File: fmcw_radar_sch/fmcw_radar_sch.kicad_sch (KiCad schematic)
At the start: 0 parts

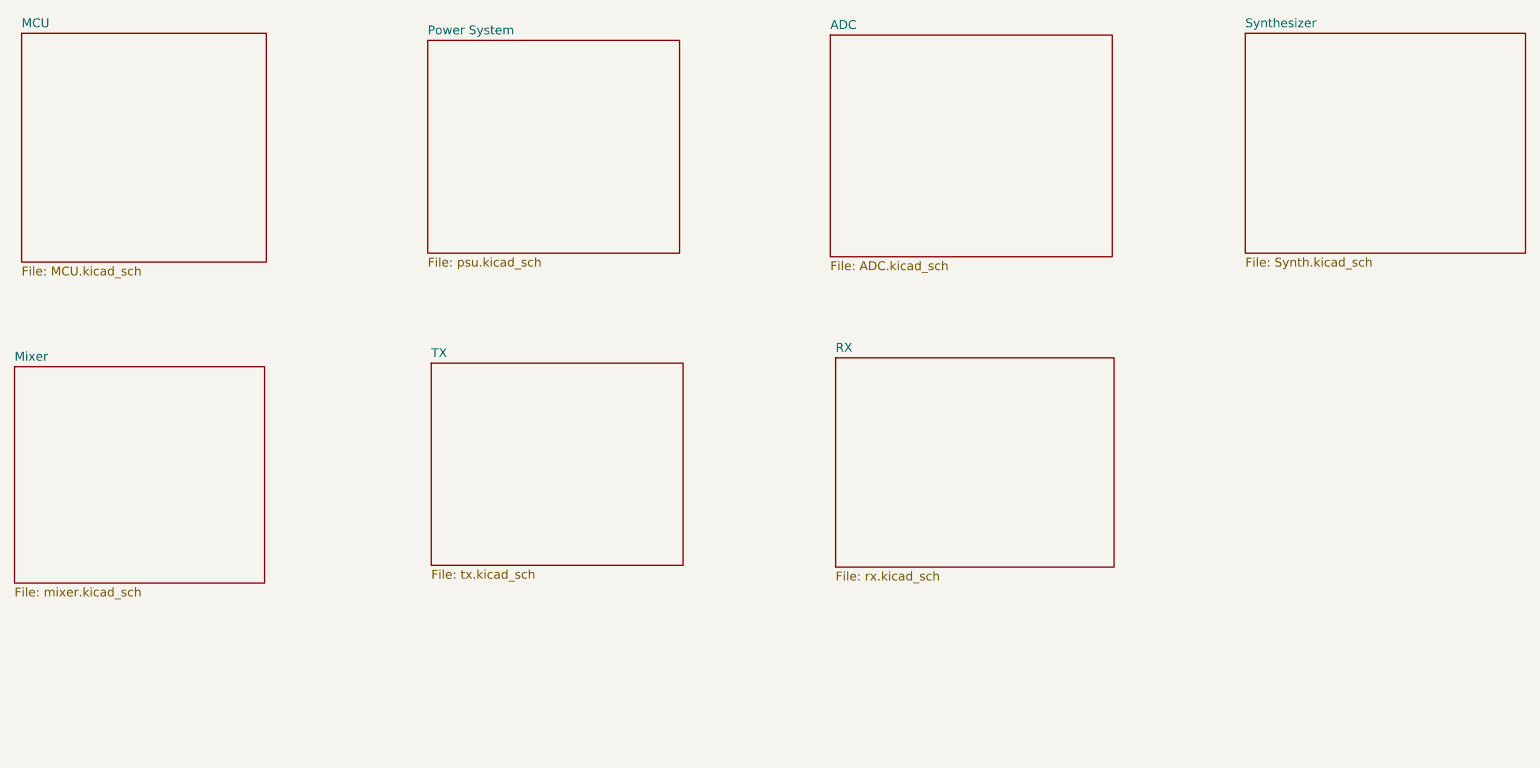
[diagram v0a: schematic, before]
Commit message: added MCU PSU VCO
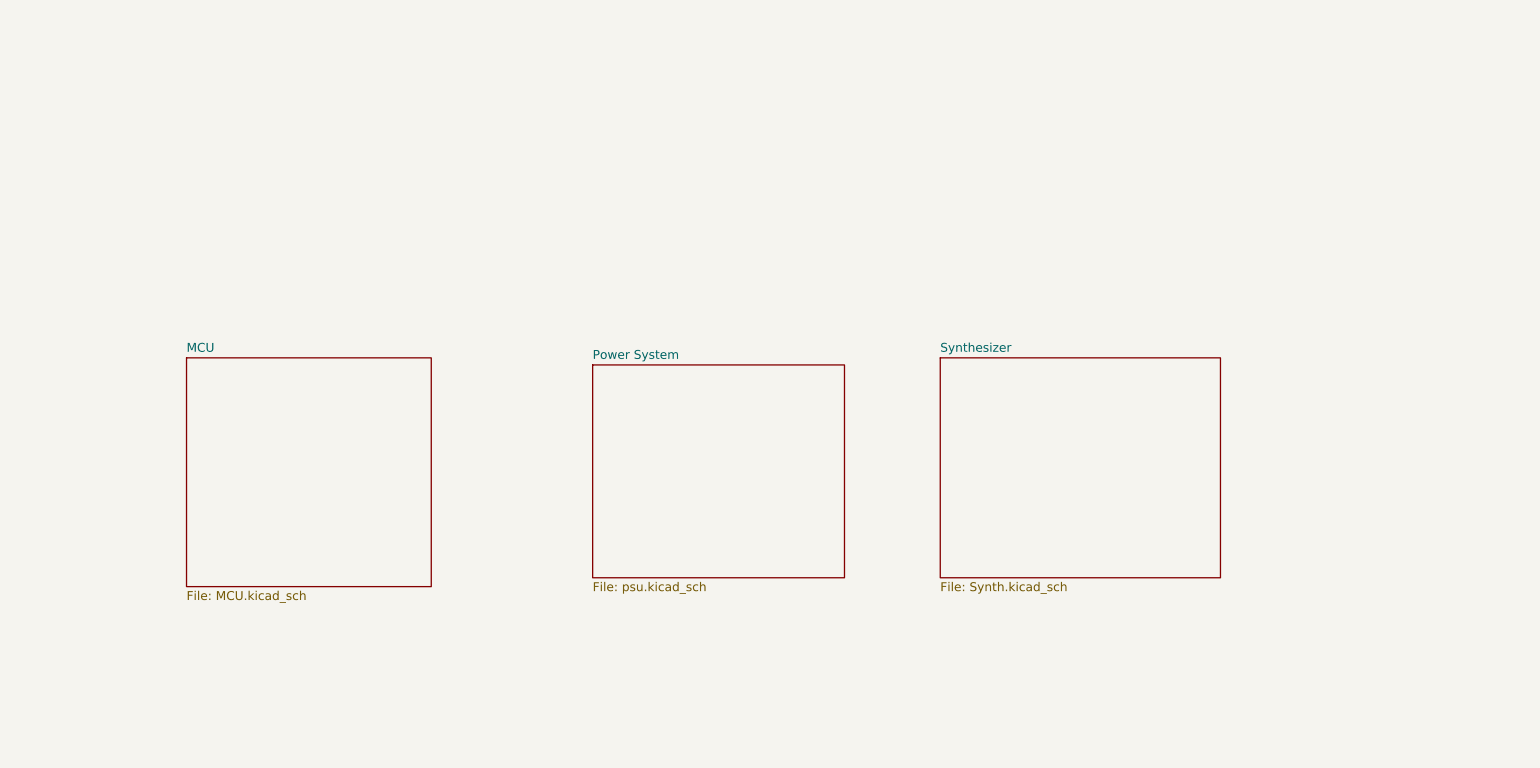
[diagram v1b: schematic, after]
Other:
- removed sheet ADC
- removed sheet Mixer
- removed sheet RX
- removed sheet TX
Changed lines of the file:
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@@
 	(paper "A4")
 	(sheet
-		(at 150.114 76.2)
-		(size 39.878 29.972)
-		(exclude_from_sim no)
-		(in_bom yes)
-		(on_board yes)
-		(dnp no)
-		(fields_autoplaced yes)
-		(stroke
-			(width 0.1524)
-			(type solid)
-		)
-		(fill
-			(color 0 0 0 0.0000)
-		)
-		(property "Sheetname" "RX"
-			(at 150.114 75.4884 0)
-			(effects
-				(font
-					(size 1.27 1.27)
-				)
-				(justify left bottom)
-			)
-		)
-		(property "Sheetfile" "rx.kicad_sch"
-			(at 150.114 106.7566 0)
-			(effects
-				(font
-					(size 1.27 1.27)
-				)
-				(justify left top)
-			)
-		)
-		(instances
-			(project "fmcw_radar_sch"
-				(path "/435eb955-ea36-4ca2-96a0-71f0d07942fb"
-					(page "8")
-				)
-			)
-		)
-	)
-	(sheet
-		(at 149.352 29.972)
-		(size 40.386 31.75)
-		(exclude_from_sim no)
-		(in_bom yes)
-		(on_board yes)
-		(dnp no)
-		(fields_autoplaced yes)
-		(stroke
-			(width 0.1524)
-			(type solid)
-		)
-		(fill
-			(color 0 0 0 0.0000)
-		)
-		(property "Sheetname" "ADC"
-			(at 149.352 29.2604 0)
-			(effects
-				(font
-					(size 1.27 1.27)
-				)
-				(justify left bottom)
-			)
-		)
-		(property "Sheetfile" "ADC.kicad_sch"
-			(at 149.352 62.3066 0)
-			(effects
-				(font
-					(size 1.27 1.27)
-				)
-				(justify left top)
-			)
-		)
-		(instances
-			(project "fmcw_radar_sch"
-				(path "/435eb955-ea36-4ca2-96a0-71f0d07942fb"
-					(page "4")
-				)
-			)
-		)
-	)
-	(sheet
-		(at 92.202 76.962)
-		(size 36.068 28.956)
-		(exclude_from_sim no)
-		(in_bom yes)
-		(on_board yes)
-		(dnp no)
-		(fields_autoplaced yes)
-		(stroke
-			(width 0.1524)
-			(type solid)
-		)
-		(fill
-			(color 0 0 0 0.0000)
-		)
-		(property "Sheetname" "TX"
-			(at 92.202 76.2504 0)
-			(effects
-				(font
-					(size 1.27 1.27)
-				)
-				(justify left bottom)
-			)
-		)
-		(property "Sheetfile" "tx.kicad_sch"
-			(at 92.202 106.5026 0)
-			(effects
-				(font
-					(size 1.27 1.27)
-				)
-				(justify left top)
-			)
-		)
-		(instances
-			(project "fmcw_radar_sch"
-				(path "/435eb955-ea36-4ca2-96a0-71f0d07942fb"
-					(page "7")
-				)
-			)
-		)
-	)
-	(sheet
-		(at 32.512 77.47)
-		(size 35.814 30.988)
-		(exclude_from_sim no)
-		(in_bom yes)
-		(on_board yes)
-		(dnp no)
-		(fields_autoplaced yes)
-		(stroke
-			(width 0.1524)
-			(type solid)
-		)
-		(fill
-			(color 0 0 0 0.0000)
-		)
-		(property "Sheetname" "Mixer"
-			(at 32.512 76.7584 0)
-			(effects
-				(font
-					(size 1.27 1.27)
-				)
-				(justify left bottom)
-			)
-		)
-		(property "Sheetfile" "mixer.kicad_sch"
-			(at 32.512 109.0426 0)
-			(effects
-				(font
-					(size 1.27 1.27)
-				)
-				(justify left top)
-			)
-		)
-		(instances
-			(project "fmcw_radar_sch"
-				(path "/435eb955-ea36-4ca2-96a0-71f0d07942fb"
-					(page "6")
-				)
-			)
-		)
-	)
-	(sheet
-		(at 33.528 29.718)
+		(at 57.15 76.2)
 		(size 35.052 32.766)
 		(exclude_from_sim no)
@@
 		)
 		(property "Sheetname" "MCU"
-			(at 33.528 29.0064 0)
+			(at 57.15 75.4884 0)
 			(effects
 				(font
@@
 		)
 		(property "Sheetfile" "MCU.kicad_sch"
-			(at 33.528 63.0686 0)
+			(at 57.15 109.5506 0)
 			(effects
 				(font
@@
 	)
 	(sheet
-		(at 208.788 29.718)
+		(at 165.1 76.2)
 		(size 40.132 31.496)
 		(exclude_from_sim no)
@@
 		)
 		(property "Sheetname" "Synthesizer"
-			(at 208.788 29.0064 0)
+			(at 165.1 75.4884 0)
 			(effects
 				(font
@@
 		)
 		(property "Sheetfile" "Synth.kicad_sch"
-			(at 208.788 61.7986 0)
+			(at 165.1 108.2806 0)
 			(effects
 				(font
@@
 	)
 	(sheet
-		(at 91.694 30.734)
+		(at 115.316 77.216)
 		(size 36.068 30.48)
 		(exclude_from_sim no)
@@
 		)
 		(property "Sheetname" "Power System"
-			(at 91.694 30.0224 0)
+			(at 115.316 76.5044 0)
 			(effects
 				(font
@@
 		)
 		(property "Sheetfile" "psu.kicad_sch"
-			(at 91.694 61.7986 0)
+			(at 115.316 108.2806 0)
 			(effects
 				(font

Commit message: board changes
board changes
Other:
- added sheet DAC (DAC.kicad_sch)
- added sheet Reciever (rx_radar.kicad_sch)
- added sheet Tx (tx_radar.kicad_sch)
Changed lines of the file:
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@@
 	(paper "A4")
 	(sheet
-		(at 57.15 76.2)
+		(at 132.334 101.854)
+		(size 41.656 25.4)
+		(exclude_from_sim no)
+		(in_bom yes)
+		(on_board yes)
+		(dnp no)
+		(fields_autoplaced yes)
+		(stroke
+			(width 0.1524)
+			(type solid)
+		)
+		(fill
+			(color 0 0 0 0.0000)
+		)
+		(property "Sheetname" "DAC"
+			(at 132.334 101.1424 0)
+			(effects
+				(font
+					(size 1.27 1.27)
+				)
+				(justify left bottom)
+			)
+		)
+		(property "Sheetfile" "DAC.kicad_sch"
+			(at 132.334 127.8386 0)
+			(effects
+				(font
+					(size 1.27 1.27)
+				)
+				(justify left top)
+			)
+		)
+		(instances
+			(project "fmcw_radar_sch"
+				(path "/435eb955-ea36-4ca2-96a0-71f0d07942fb"
+					(page "7")
+				)
+			)
+		)
+	)
+	(sheet
+		(at 45.974 102.362)
+		(size 34.544 27.94)
+		(exclude_from_sim no)
+		(in_bom yes)
+		(on_board yes)
+		(dnp no)
+		(fields_autoplaced yes)
+		(stroke
+			(width 0.1524)
+			(type solid)
+		)
+		(fill
+			(color 0 0 0 0.0000)
+		)
+		(property "Sheetname" "Tx"
+			(at 45.974 101.6504 0)
+			(effects
+				(font
+					(size 1.27 1.27)
+				)
+				(justify left bottom)
+			)
+		)
+		(property "Sheetfile" "tx_radar.kicad_sch"
+			(at 45.974 130.8866 0)
+			(effects
+				(font
+					(size 1.27 1.27)
+				)
+				(justify left top)
+			)
+		)
+		(pin "Vpos" input
+			(at 45.974 110.236 180)
+			(effects
+				(font
+					(size 1.27 1.27)
+				)
+				(justify left)
+			)
+		)
+		(pin "Vpos1" input
+			(at 45.974 112.776 180)
+			(effects
+				(font
+					(size 1.27 1.27)
+				)
+				(justify left)
+			)
+		)
+		(pin "Vpos3" input
+			(at 45.974 115.316 180)
+			(effects
+				(font
+					(size 1.27 1.27)
+				)
+				(justify left)
+			)
+		)
+		(pin "Vpos4" input
+			(at 45.974 117.856 180)
+			(effects
+				(font
+					(size 1.27 1.27)
+				)
+				(justify left)
+			)
+		)
+		(instances
+			(project "fmcw_radar_sch"
+				(path "/435eb955-ea36-4ca2-96a0-71f0d07942fb"
+					(page "5")
+				)
+			)
+		)
+	)
+	(sheet
+		(at 43.434 50.546)
 		(size 35.052 32.766)
 		(exclude_from_sim no)
@@
 		)
 		(property "Sheetname" "MCU"
-			(at 57.15 75.4884 0)
+			(at 43.434 49.8344 0)
 			(effects
 				(font
@@
 		)
 		(property "Sheetfile" "MCU.kicad_sch"
-			(at 57.15 109.5506 0)
+			(at 43.434 83.8966 0)
 			(effects
 				(font
@@
 	)
 	(sheet
-		(at 165.1 76.2)
+		(at 130.81 49.53)
 		(size 40.132 31.496)
 		(exclude_from_sim no)
@@
 		)
 		(property "Sheetname" "Synthesizer"
-			(at 165.1 75.4884 0)
+			(at 130.81 48.8184 0)
 			(effects
 				(font
@@
 		)
 		(property "Sheetfile" "Synth.kicad_sch"
-			(at 165.1 108.2806 0)
+			(at 130.81 81.6106 0)
 			(effects
 				(font
@@
 	)
 	(sheet
-		(at 115.316 77.216)
+		(at 88.138 50.292)
 		(size 36.068 30.48)
 		(exclude_from_sim no)
@@
 		)
 		(property "Sheetname" "Power System"
-			(at 115.316 76.5044 0)
+			(at 88.138 49.5804 0)
 			(effects
 				(font
@@
 		)
 		(property "Sheetfile" "psu.kicad_sch"
-			(at 115.316 108.2806 0)
+			(at 88.138 81.3566 0)
 			(effects
 				(font
@@
 				)
 			)
+		)
+	)
+	(sheet
+		(at 87.63 101.6)
+		(size 36.83 27.94)
+		(exclude_from_sim no)
+		(in_bom yes)
+		(on_board yes)
+		(dnp no)
+		(fields_autoplaced yes)
+		(stroke
+			(width 0.1524)
+			(type solid)
+		)
+		(fill
+			(color 0 0 0 0.0000)
+		)
+		(property "Sheetname" "Reciever"
+			(at 87.63 100.8884 0)
+			(effects
+				(font
+					(size 1.27 1.27)
+				)
+				(justify left bottom)
+			)
+		)
+		(property "Sheetfile" "rx_radar.kicad_sch"
+			(at 87.63 130.1246 0)
+			(effects
+				(font
+					(size 1.27 1.27)
+				)
+				(justify left top)
+			)
+		)
+		(instances
+			(project "fmcw_radar_sch"
+				(path "/435eb955-ea36-4ca2-96a0-71f0d07942fb"
+					(page "6")
+				)
+			)

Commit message: changes
changes
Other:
- removed sheet Reciever
- removed sheet Synthesizer
- removed sheet Tx
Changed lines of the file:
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@@
 	(paper "A4")
 	(sheet
-		(at 132.334 101.854)
-		(size 41.656 25.4)
+		(at 132.08 51.308)
+		(size 45.72 28.448)
 		(exclude_from_sim no)
 		(in_bom yes)
@@
 		)
 		(property "Sheetname" "DAC"
-			(at 132.334 101.1424 0)
+			(at 132.08 50.5964 0)
 			(effects
 				(font
@@
 		)
 		(property "Sheetfile" "DAC.kicad_sch"
-			(at 132.334 127.8386 0)
+			(at 132.08 80.3406 0)
 			(effects
 				(font
@@
 				(path "/435eb955-ea36-4ca2-96a0-71f0d07942fb"
 					(page "7")
-				)
-			)
-		)
-	)
-	(sheet
-		(at 45.974 102.362)
-		(size 34.544 27.94)
-		(exclude_from_sim no)
-		(in_bom yes)
-		(on_board yes)
-		(dnp no)
-		(fields_autoplaced yes)
-		(stroke
-			(width 0.1524)
-			(type solid)
-		)
-		(fill
-			(color 0 0 0 0.0000)
-		)
-		(property "Sheetname" "Tx"
-			(at 45.974 101.6504 0)
-			(effects
-				(font
-					(size 1.27 1.27)
-				)
-				(justify left bottom)
-			)
-		)
-		(property "Sheetfile" "tx_radar.kicad_sch"
-			(at 45.974 130.8866 0)
-			(effects
-				(font
-					(size 1.27 1.27)
-				)
-				(justify left top)
-			)
-		)
-		(pin "Vpos" input
-			(at 45.974 110.236 180)
-			(effects
-				(font
-					(size 1.27 1.27)
-				)
-				(justify left)
-			)
-		)
-		(pin "Vpos1" input
-			(at 45.974 112.776 180)
-			(effects
-				(font
-					(size 1.27 1.27)
-				)
-				(justify left)
-			)
-		)
-		(pin "Vpos3" input
-			(at 45.974 115.316 180)
-			(effects
-				(font
-					(size 1.27 1.27)
-				)
-				(justify left)
-			)
-		)
-		(pin "Vpos4" input
-			(at 45.974 117.856 180)
-			(effects
-				(font
-					(size 1.27 1.27)
-				)
-				(justify left)
-			)
-		)
-		(instances
-			(project "fmcw_radar_sch"
-				(path "/435eb955-ea36-4ca2-96a0-71f0d07942fb"
-					(page "5")
 				)
 			)
@@
 	)
 	(sheet
-		(at 130.81 49.53)
-		(size 40.132 31.496)
-		(exclude_from_sim no)
-		(in_bom yes)
-		(on_board yes)
-		(dnp no)
-		(fields_autoplaced yes)
-		(stroke
-			(width 0.1524)
-			(type solid)
-		)
-		(fill
-			(color 0 0 0 0.0000)
-		)
-		(property "Sheetname" "Synthesizer"
-			(at 130.81 48.8184 0)
-			(effects
-				(font
-					(size 1.27 1.27)
-				)
-				(justify left bottom)
-			)
-		)
-		(property "Sheetfile" "Synth.kicad_sch"
-			(at 130.81 81.6106 0)
-			(effects
-				(font
-					(size 1.27 1.27)
-				)
-				(justify left top)
-			)
-		)
-		(instances
-			(project "fmcw_radar_sch"
-				(path "/435eb955-ea36-4ca2-96a0-71f0d07942fb"
-					(page "5")
-				)
-			)
-		)
-	)
-	(sheet
 		(at 88.138 50.292)
 		(size 36.068 30.48)
@@
 				)
 			)
-		)
-	)
-	(sheet
-		(at 87.63 101.6)
-		(size 36.83 27.94)
-		(exclude_from_sim no)
-		(in_bom yes)
-		(on_board yes)
-		(dnp no)
-		(fields_autoplaced yes)
-		(stroke
-			(width 0.1524)
-			(type solid)
-		)
-		(fill
-			(color 0 0 0 0.0000)
-		)
-		(property "Sheetname" "Reciever"
-			(at 87.63 100.8884 0)
-			(effects
-				(font
-					(size 1.27 1.27)
-				)
-				(justify left bottom)
-			)
-		)
-		(property "Sheetfile" "rx_radar.kicad_sch"
-			(at 87.63 130.1246 0)
-			(effects
-				(font
-					(size 1.27 1.27)
-				)
-				(justify left top)
-			)
-		)
-		(instances
-			(project "fmcw_radar_sch"
-				(path "/435eb955-ea36-4ca2-96a0-71f0d07942fb"
-					(page "6")
-				)
-			)

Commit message: final changes to RF board
final changes to RF board + grbs
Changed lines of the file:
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@@
 	(sheet
 		(at 132.08 51.308)
-		(size 45.72 28.448)
+		(size 32.258 28.448)
 		(exclude_from_sim no)
 		(in_bom yes)
